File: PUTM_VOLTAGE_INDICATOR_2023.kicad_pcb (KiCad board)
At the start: 2 copper layers, 35 parts, among them IC1 LM211DT, J1 HV+, J2 HV-, Q1 TK3P80E,RQ, U1 LT8316EFE

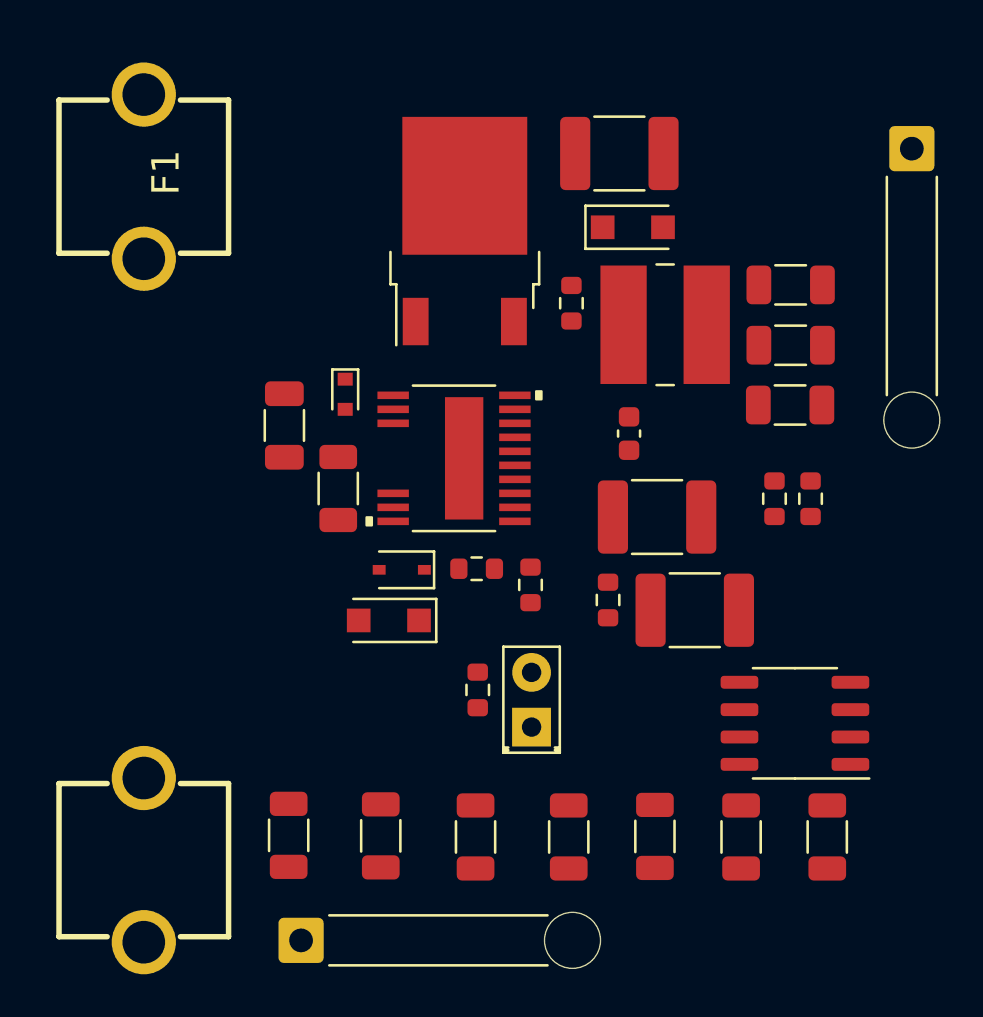
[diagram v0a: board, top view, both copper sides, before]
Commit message: pcb update
Changed converter layout, fuse footprint
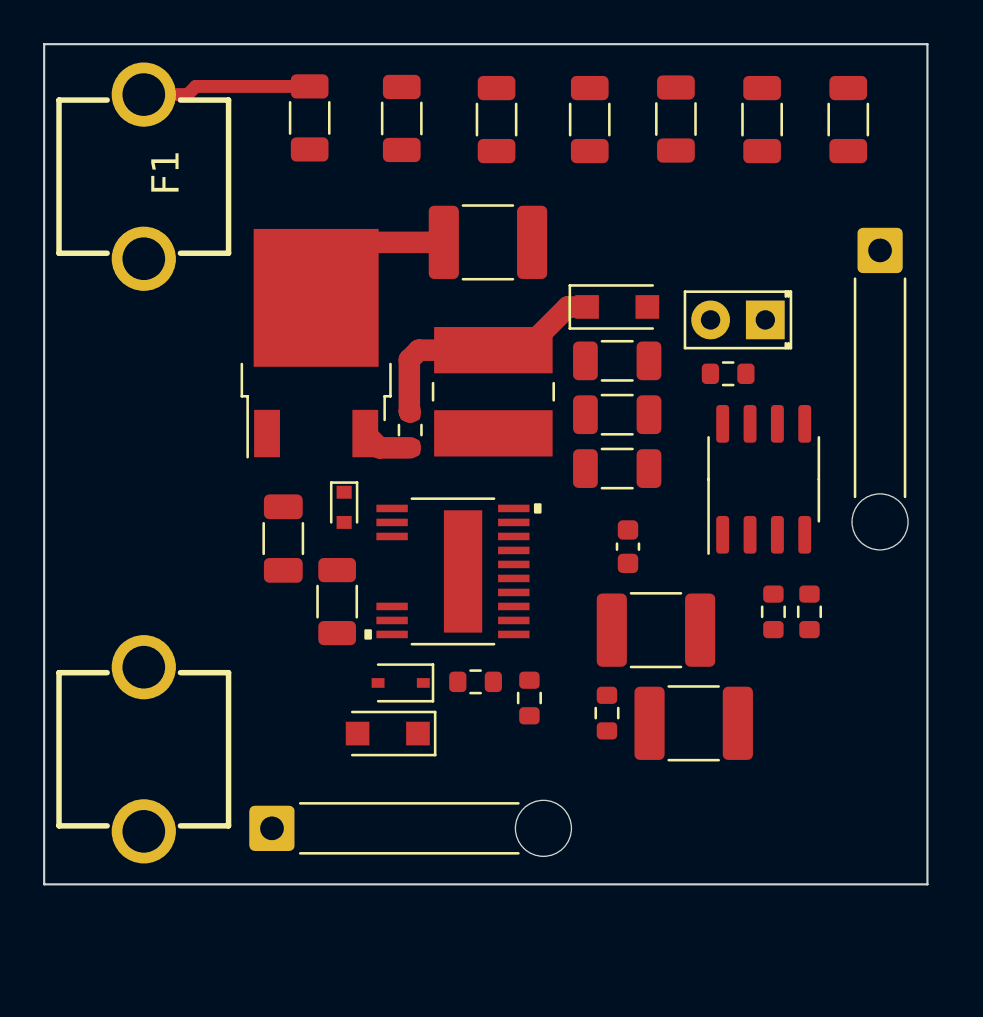
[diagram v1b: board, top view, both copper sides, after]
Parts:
- moved R3 33.3 mm to (114.0, 99.5)
- moved R4 33.3 mm to (118.3, 99.5)
- moved R5 33.3 mm to (122.3, 99.5)
- moved R6 33.3 mm to (126.3, 99.5)
- moved R7 33.3 mm to (130.3, 99.5)
- moved R1 33.3 mm to (105.3, 99.4)
- moved R2 33.3 mm to (109.6, 99.5)
- moved D1 21.8 mm to (126.5, 108.8), turned to 180 degrees
- moved R14 18.7 mm to (124.8, 111.3), turned to 180 degrees
- moved IC1 11.4 mm to (126.4, 116.2), turned to 90 degrees
- moved R19 9.52 mm to (110.0, 113.9)
- moved C8 8.79 mm to (119.6, 110.7)
- moved C7 8.67 mm to (119.6, 113.2)
- moved Q1 8.64 mm to (105.6, 109.9)
- moved L1 8.56 mm to (113.9, 112.1), turned to -90 degrees
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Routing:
- net +VDC: track 0.00 -> 15.0 mm
- net Net-(C1-Pad2): track 0.00 -> 11.7 mm
- net Net-(Q1-Pad3): track 0.00 -> 2.36 mm
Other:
- board outline added: 41 x 39 mm
